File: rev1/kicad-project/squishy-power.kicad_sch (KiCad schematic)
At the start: 99 parts, among them SW1 RST, U1 THVD1452DGSR, U10 THVD1452DGSR, U11 FXL4TD245BQX, U13 THVD1452DGSR, U15 THVD1452DGSR, U16 FXL4TD245BQX, U17 THVD1452DGSR, U18 THVD1452DGSR, U2 FXL4TD245BQX, U20 FXL4TD245BQX, U21 THVD1452DGSR, U22 THVD1452DGSR, U23 FXL4TD245BQX, U24 THVD1452DGSR, U25 THVD1452DGSR, U26 W25N01GVZEIG, U27 FXL4TD245BQX, U28 THVD1452DGSR, U29 THVD1452DGSR, U3 TLV755533PDRVR, U30 FXL4TD245BQX, U31 THVD1452DGSR, U32 THVD1452DGSR, U33 FXL4TD245BQX, U34 THVD1452DGSR, U35 APX811-40UG-7, U4 THVD1452DGSR, U5 TLV73312PQDRVRQ1, U6 THVD1452DGSR, U7 LP5910-1.8DRVR, U8 FXL4TD245BQX, U9 THVD1452DGSR

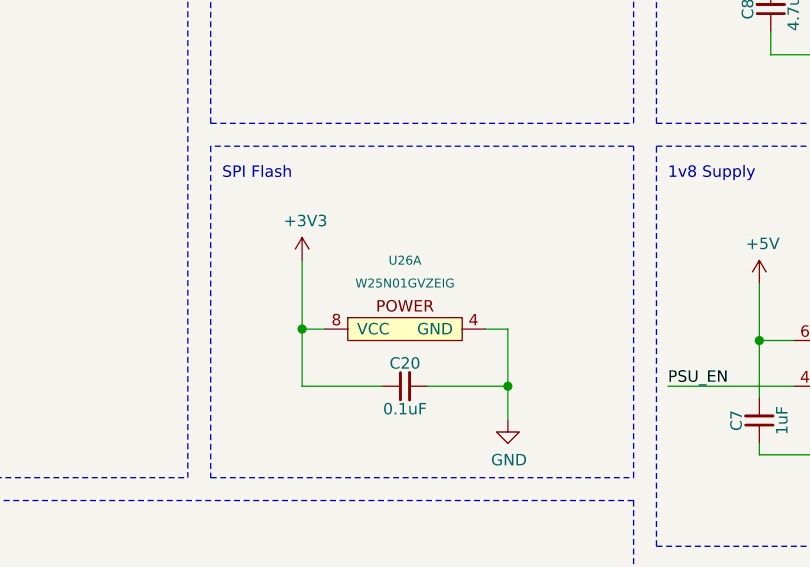
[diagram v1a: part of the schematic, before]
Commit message: hardware: rev1: Updated the SPI flash and ULPI osc, this closes #2
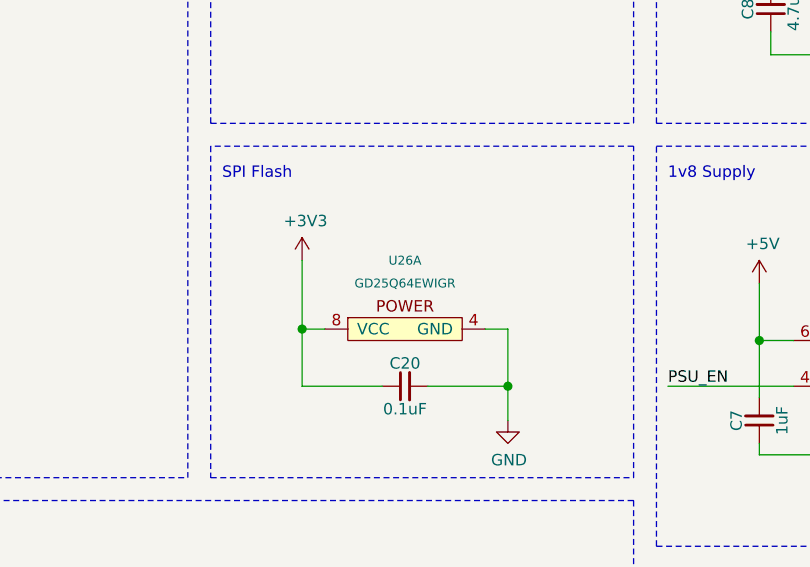
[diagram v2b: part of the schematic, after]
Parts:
- U26: value W25N01GVZEIG -> GD25Q64EWIGR; footprint lethalbit-memory:WSON-8-1EP-6.0x8.0mm -> rhais_package-qfn:UDFN-8-1EP_6x5mm_P1.27mm_EP3.4x4mm; MFR Winbond -> GigaDevice; MPN W25N01GVZEIG TR -> GD25Q64EWIGR
